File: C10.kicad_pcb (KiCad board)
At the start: 2 copper layers, 90.3 x 26.5 mm, 73 parts, among them IC3 74HC595BQ,115, J1 USB_B_Mini, J2 Conn_01x16_Male, J3 Conn_01x06, J4 UPDI, J5 Conn_01x08_Male, U2 ATmega4809-M, U5 MIC5205-3.3YM5, U6 FT230XQ, U7 ISO7742, X1 ASE-24MHz

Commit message: Initial commit
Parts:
- IC3: footprint _Samac:74HC595BQ115 -> RTB_foot:74HC595BQ115
- J1: footprint _Samac:USB_Micro-B_Reichelt_BWM_SMD -> RTB:USB_Micro-B_Reichelt_BWM_SMD

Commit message: Initial commit
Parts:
- D1: value D -> 1N4148
- R22, R23, R5: value 100k -> 3.3k
- R28: value 120k -> 3.3k
- U2: value ATmega4809-M -> AVR64DA48

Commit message: initial
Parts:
- added C17: 100n, Capacitor_SMD:C_0603_1608Metric, B.Cu at (144.1, 31.8)
- added C19: 220u/6V, Capacitor_SMD:C_1206_3216Metric, B.Cu at (136.3, 31.8)
- added C20: 220u/6V, Capacitor_SMD:C_1206_3216Metric, B.Cu at (131.6, 31.8)
- added D6: LED(red), LED_SMD:LED_0603_1608Metric, F.Cu at (151.9, 32.5)
- added IC1: TPS2552DRVT, RTB:SON65P200X200X80-7N, B.Cu at (141.7, 31.9)
- added JP3: USB power, Connector_PinHeader_2.54mm:PinHeader_1x02_P2.54mm_Vertical, F.Cu at (127.0, 31.2)
- added L2: Ferrite_Bead, Inductor_SMD:L_0805_2012Metric, B.Cu at (148.1, 32.4)
- added R10: 22k, Resistor_SMD:R_0603_1608Metric, B.Cu at (139.3, 31.5)
- added R12: 1k, Resistor_SMD:R_0603_1608Metric, B.Cu at (151.9, 32.5)
- added R9: 100k, Resistor_SMD:R_0603_1608Metric, B.Cu at (145.6, 31.8)
- moved D1 14.2 mm to (119.2, 34.2), turned to 90 degrees
- moved C3 7.18 mm to (121.2, 36.1), turned to 90 degrees
- moved C2 5.95 mm to (126.6, 36.1), turned to 270 degrees
- moved C16 4.94 mm to (121.3, 40.5), turned to 180 degrees
- moved U5 3.77 mm to (123.9, 36.1), turned to 270 degrees
- turned L1 to 90 degrees
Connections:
- net /USB/VBUS renamed VBUS
- J2 pad 11: (no net) -> GNDS
- J2 pad 12: (no net) -> GNDS
- J2 pad 13: (no net) -> VEXT
- J2 pad 14: (no net) -> VEXT
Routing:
- net 3.3V: track 37.0 -> 92.2 mm, vias 10 -> 22
- net Vrail: track 20.5 -> 39.0 mm, vias 0 -> 1
- net Net-(C19-Pad1): track 0.00 -> 16.0 mm
- net Net-(D6-Pad1): track 0.00 -> 14.0 mm, vias 0 -> 1
- net VBUS: track 21.5 -> 30.6 mm, vias 1 -> 4
- net GNDS: track 28.8 -> 36.6 mm, vias 6 -> 9
- net VEXT: track 0.00 -> 5.55 mm
- net Net-(J1-Pad6): track 18.2 -> 23.3 mm
- net Net-(C17-Pad1): track 0.00 -> 4.40 mm
- net Net-(IC1-Pad4): track 0.00 -> 4.11 mm
- net GNDD: track 44.3 -> 41.9 mm
- net VCCIO: track 19.5 -> 17.6 mm, vias 3 -> 1
- net Net-(IC1-Pad2): track 0.00 -> 1.53 mm
- net Net-(C16-Pad1): track 15.5 -> 14.3 mm
- net Net-(D6-Pad2): vias 0 -> 1
- added copper zone on B.Cu, net GNDS
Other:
- rule pad_to_mask_clearance: 0.2 -> 0
- board text added: "FS'24"
- board text added: "Ovld"
- board text added: "RTB domain"
- board text added: "RTB.master C10.4"
- board text added: "USB"
- board text added: "USB domain"
- board text added: "USB power close"
- board text removed: "FS'23"
- board text removed: "RTB.master C10.3"

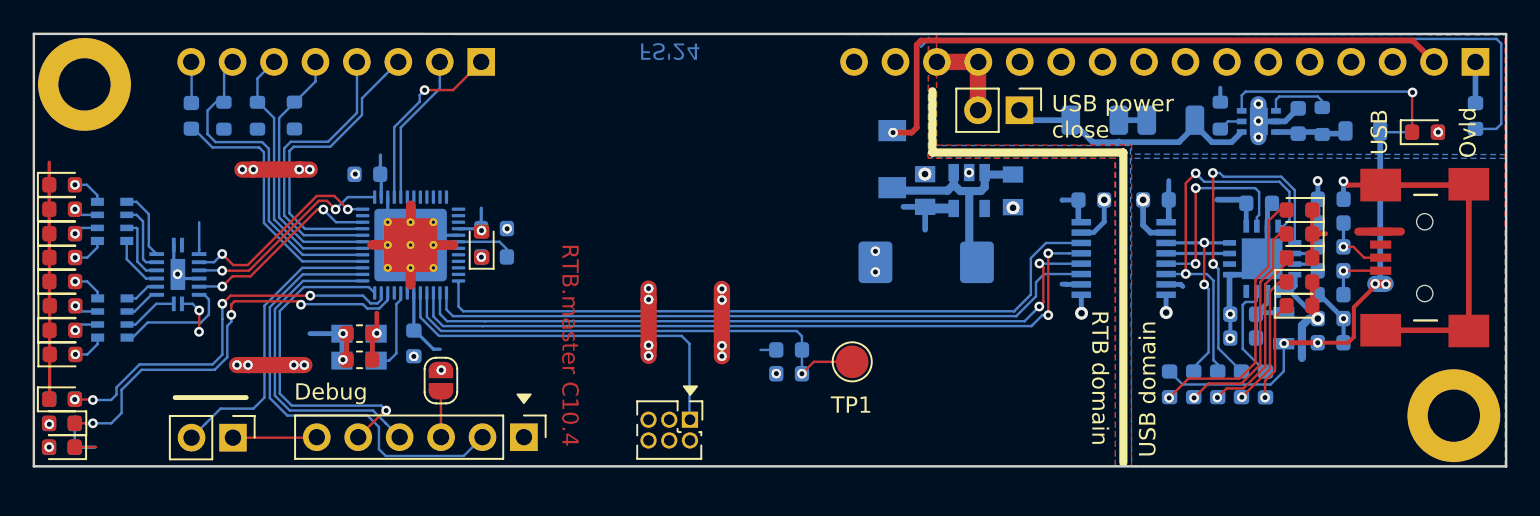
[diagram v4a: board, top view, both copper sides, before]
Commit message: mod: optimized for PCB assembly
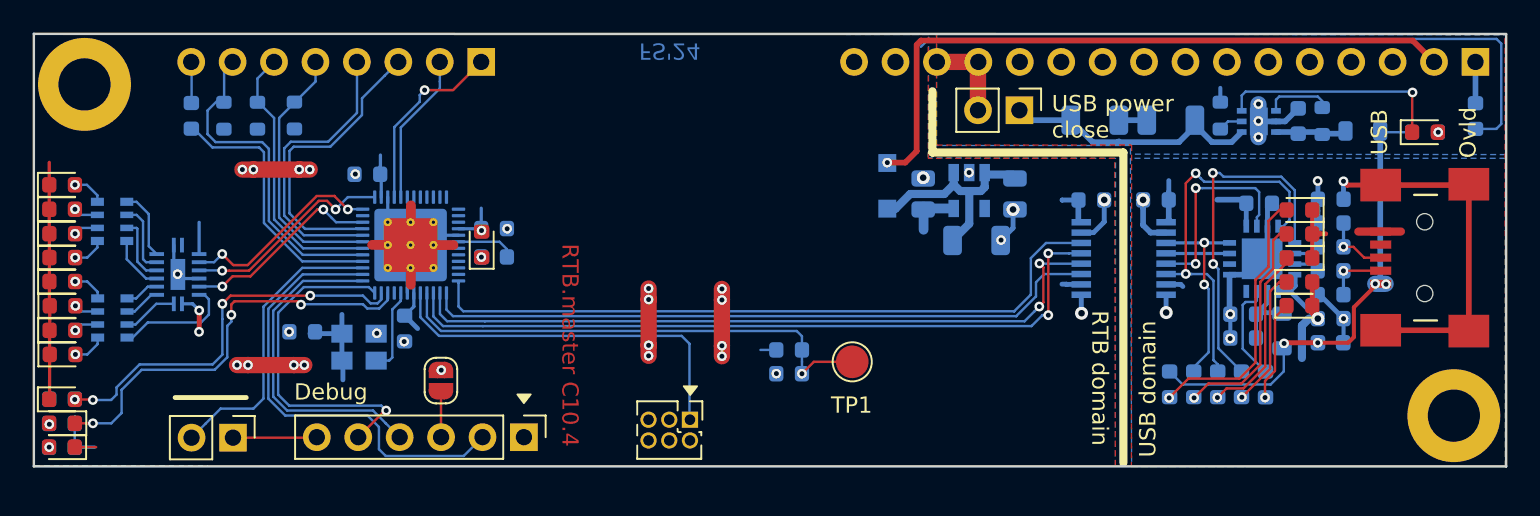
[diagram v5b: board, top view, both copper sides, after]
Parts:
- removed C1: 2.2u, Capacitor_SMD:C_0603_1608Metric
- C10, C17, C22, C4, C7, C9: value 100n -> 100nF
- C11: value 100n -> 100nF; moved to B.Cu
- C12, C13, C18, C8: value 1u -> 100nF
- C14, C15: value 47p -> 47pF
- C16: value 100uF/25V -> 22uF/25V; footprint Capacitor_Tantalum_SMD:CP_EIA-7343-43_Kemet-X -> Capacitor_SMD:C_1206_3216Metric
- C19, C20: value 220u/6V -> 220u/6.3V
- C2: value 47uF/25V -> 100nF/50V; footprint Capacitors_SMD:C_0805 -> Capacitor_SMD:C_0805_2012Metric
- C3: value 4.7uF/10V -> 10uF/25V; footprint Capacitors_SMD:C_0805 -> Capacitor_SMD:C_0805_2012Metric
- C5: value 100n -> 100nF; footprint Resistor_SMD:R_0603_1608Metric -> Capacitor_SMD:C_0603_1608Metric
- C6: value 4.7u/25V -> 4.7uF
- D1: value 1N4148 -> BAS16H,115; footprint Diode_SMD:D_MiniMELF -> Diode_SMD:D_SOD-123F
- D11, D12: value LED_grn -> LED(grn)
- D14, D32, D33, D34, D35, D36, D37: value LED_Small -> LED(wht)
- D17: value RTS_red -> RTS(red)
- D18: value CTS_red -> CTS(red)
- D2: value Locate(blu) -> Locate(blue)
- D5: value LED(grn) -> PWR(grn)
- D6: value LED(red) -> Alarm(pink)
- D8: value PWR_grn -> PWR(grn)
- J3: value Conn_01x06 -> Debug IF
- L1: footprint Inductors_SMD:L_0805 -> Inductor_SMD:L_0805_2012Metric
- R10: value 22k -> 27k
- R11: value 100k -> 3.3k
- R15: value 120k -> 3.3k
- R29, R30: value 4.7k -> 3.3k
- R4: value 10k -> 3.3k
- RN3, RN4: value 3.3k -> 4.7k
- moved C11 3.52 mm to (83.0, 44.8), turned to 180 degrees
- moved C16 3.37 mm to (124.4, 39.1), turned to 0 degrees
- moved D1 1.66 mm to (118.9, 35.8)
- moved C12 1.07 mm to (89.3, 44.5)
- moved C3 0.24 mm to (121.1, 36.3)
- moved C2 0.22 mm to (126.7, 36.3)
- moved L1 0.20 mm to (143.1, 44.7)
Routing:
- net 3.3V: track 92.2 -> 90.1 mm, vias 22 -> 20
- net Vrail: track 39.0 -> 41.0 mm
- net GNDD: track 41.9 -> 41.1 mm
- net Net-(C16-Pad1): track 14.3 -> 13.6 mm

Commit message: upgrade to Kicad 9
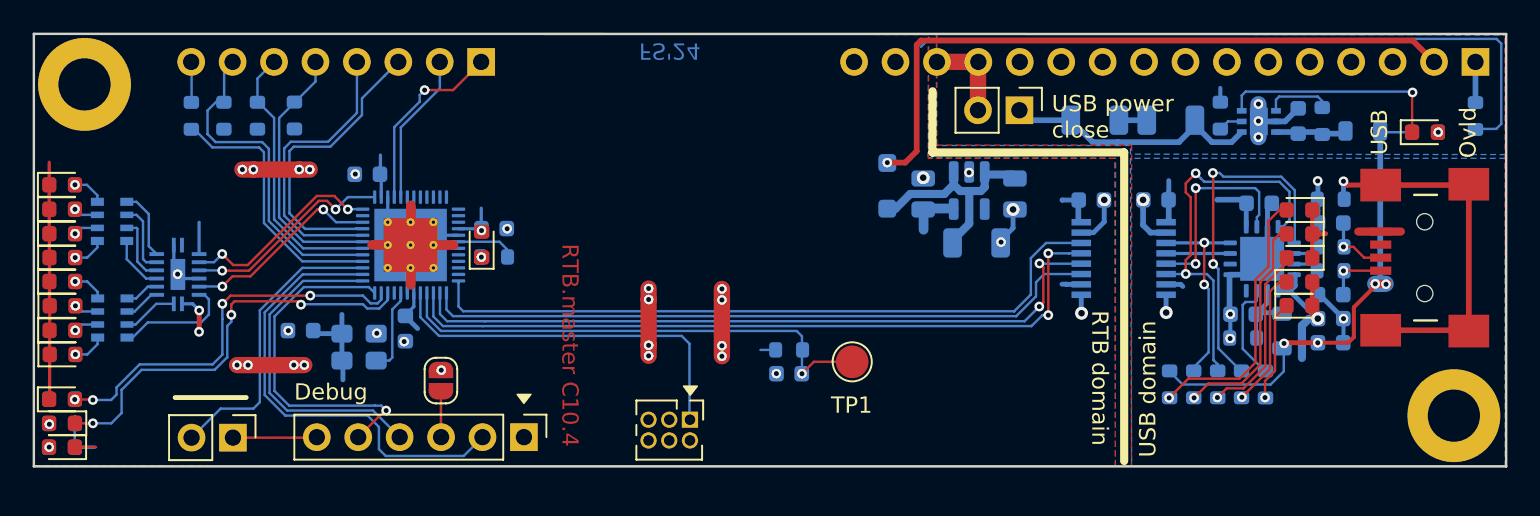
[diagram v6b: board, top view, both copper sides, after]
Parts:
- IC1: value TPS2552DRVT -> TPS2553DRVT
- IC3: footprint RTB_foot:74HC595BQ115 -> RTB:74HC595BQ115
- R10: value 27k -> 18k
- U5: footprint TO_SOT_Packages_SMD:SOT-23-5 -> Package_TO_SOT_SMD:SOT-23-5
- U6: footprint Housings_DFN_QFN:QFN-16-1EP_4x4mm_Pitch0.65mm -> Package_DFN_QFN:QFN-16-1EP_4x4mm_P0.65mm_EP2.7x2.7mm
- U7: footprint Housings_SSOP:SSOP-16_3.9x4.9mm_Pitch0.635mm -> Package_SO:SSOP-16_3.9x4.9mm_P0.635mm
- moved C16 0.15 mm to (124.4, 39.3)
- moved C11 0.13 mm to (82.9, 44.7)
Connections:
- net ~BUS.bsi renamed ~{BUS.bsi}
- net ~BUS.bso renamed ~{BUS.bso}
- net ~USB.CTS renamed ~{USB.CTS}
- net ~USB.RTS renamed ~{USB.RTS}
- net ~V24.CTS renamed ~{V24.CTS}
- net ~V24.RTS renamed ~{V24.RTS}
- IC3 pad 9: (no net) -> unconnected-(IC3-Q7S-Pad9)
- J1 pad 4: (no net) -> unconnected-(J1-ID-Pad4)
- J2 pad 10: (no net) -> unconnected-(J2-Pin_10-Pad10)
- J2 pad 3: (no net) -> unconnected-(J2-Pin_3-Pad3)
- J2 pad 4: (no net) -> unconnected-(J2-Pin_4-Pad4)
- J2 pad 5: (no net) -> unconnected-(J2-Pin_5-Pad5)
- J2 pad 6: (no net) -> unconnected-(J2-Pin_6-Pad6)
- J2 pad 7: (no net) -> unconnected-(J2-Pin_7-Pad7)
- J2 pad 8: (no net) -> unconnected-(J2-Pin_8-Pad8)
- J2 pad 9: (no net) -> unconnected-(J2-Pin_9-Pad9)
- J4 pad 3: (no net) -> unconnected-(J4-Pin_3-Pad3)
- J4 pad 4: (no net) -> unconnected-(J4-Pin_4-Pad4)
- J4 pad 5: (no net) -> unconnected-(J4-Pin_5-Pad5)
- U2 pad 11: (no net) -> unconnected-(U2-PC1-Pad11)
- U2 pad 18: (no net) -> unconnected-(U2-PC6-Pad18)
- U2 pad 19: (no net) -> unconnected-(U2-PC7-Pad19)
- U2 pad 20: (no net) -> unconnected-(U2-PD0-Pad20)
- U2 pad 21: (no net) -> unconnected-(U2-PD1-Pad21)
- U2 pad 22: (no net) -> unconnected-(U2-PD2-Pad22)
- U2 pad 23: (no net) -> unconnected-(U2-PD3-Pad23)
- U2 pad 24: (no net) -> unconnected-(U2-PD4-Pad24)
- U2 pad 25: (no net) -> unconnected-(U2-PD5-Pad25)
- U2 pad 26: (no net) -> unconnected-(U2-PD6-Pad26)
- U2 pad 27: (no net) -> unconnected-(U2-PD7-Pad27)
- U2 pad 31: (no net) -> unconnected-(U2-PE1-Pad31)
- U2 pad 32: (no net) -> unconnected-(U2-PE2-Pad32)
- U2 pad 33: (no net) -> unconnected-(U2-PE3-Pad33)
- U2 pad 34: (no net) -> unconnected-(U2-PF0-Pad34)
- U2 pad 35: (no net) -> unconnected-(U2-PF1-Pad35)
- U2 pad 45: (no net) -> unconnected-(U2-PA1-Pad45)
- U5 pad 4: (no net) -> unconnected-(U5-BP-Pad4)
- U6 pad 12: (no net) -> unconnected-(U6-CBUS0-Pad12)
- U6 pad 14: (no net) -> unconnected-(U6-CBUS3-Pad14)
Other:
- net class Default removed
- net class Power removed

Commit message: mod: part #
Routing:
- net GNDS: track 36.6 -> 34.8 mm

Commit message: update: JLCPCB parts
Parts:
- R10: value 18k -> 22k
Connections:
- IC3 pad 17: GNDD -> unconnected-(IC3-GND-Pad17)
